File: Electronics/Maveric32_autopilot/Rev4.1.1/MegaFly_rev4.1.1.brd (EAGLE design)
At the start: 69.2 x 38 mm, 115 parts, among them J1 SOLDER_JUMPER_2WAY, J2 SOLDER_JUMPER_2WAY, J3 SOLDER_JUMPER_2WAY, P1 POWER, P10 POWERSMALL_SMD, P11 POWERSMALL_SMD, P12 POWERSMALL_SMD, P13 POWERSMALL_SMD, P2 AVR32_JTAG+SERIALMOLEX_PICOBL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, P5 SPEKTRUM_RECEIVER, P6 SPEKTRUM_RECEIVER, P8 SENSOR, P9 SENSOR, Q1 N-CHANNEL_SOT23, Q2 N-CHANNEL_SOT23, Q3 N-CHANNEL_SOT23, Q4 N-CHANNEL_SOT23, Q5 MOSFET-PCHANNELSMD, U1 LM2734, U10 AT32UC3C1512/1256/1128, U2 MC78L05, U3 V_REG_MIC5235-3.3, U4 LM2734, U50 BMP180, U60 HMC5883L, U70 LSM330DLC, X1 CRYSTAL:ABM_16MHz

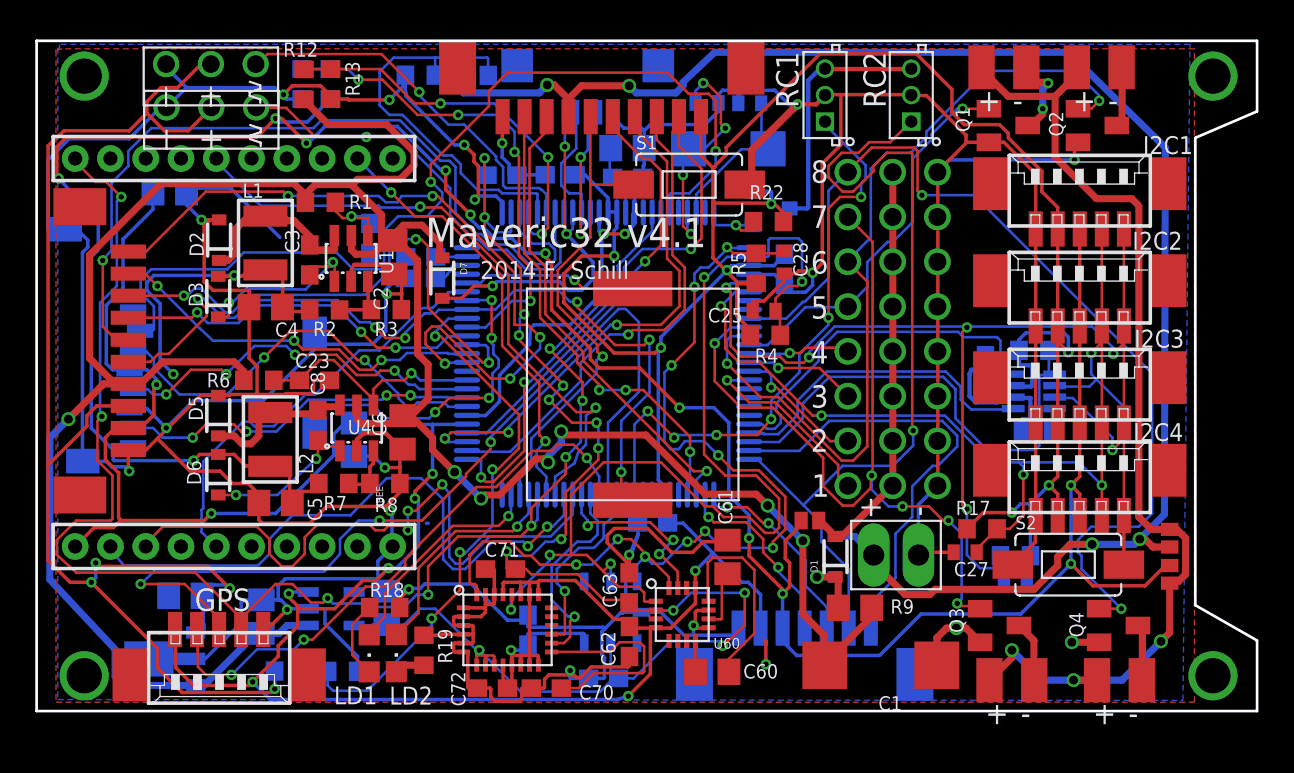
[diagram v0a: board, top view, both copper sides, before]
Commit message: New headers for communication folder of the Library and Update of Electronics for 4.1.1
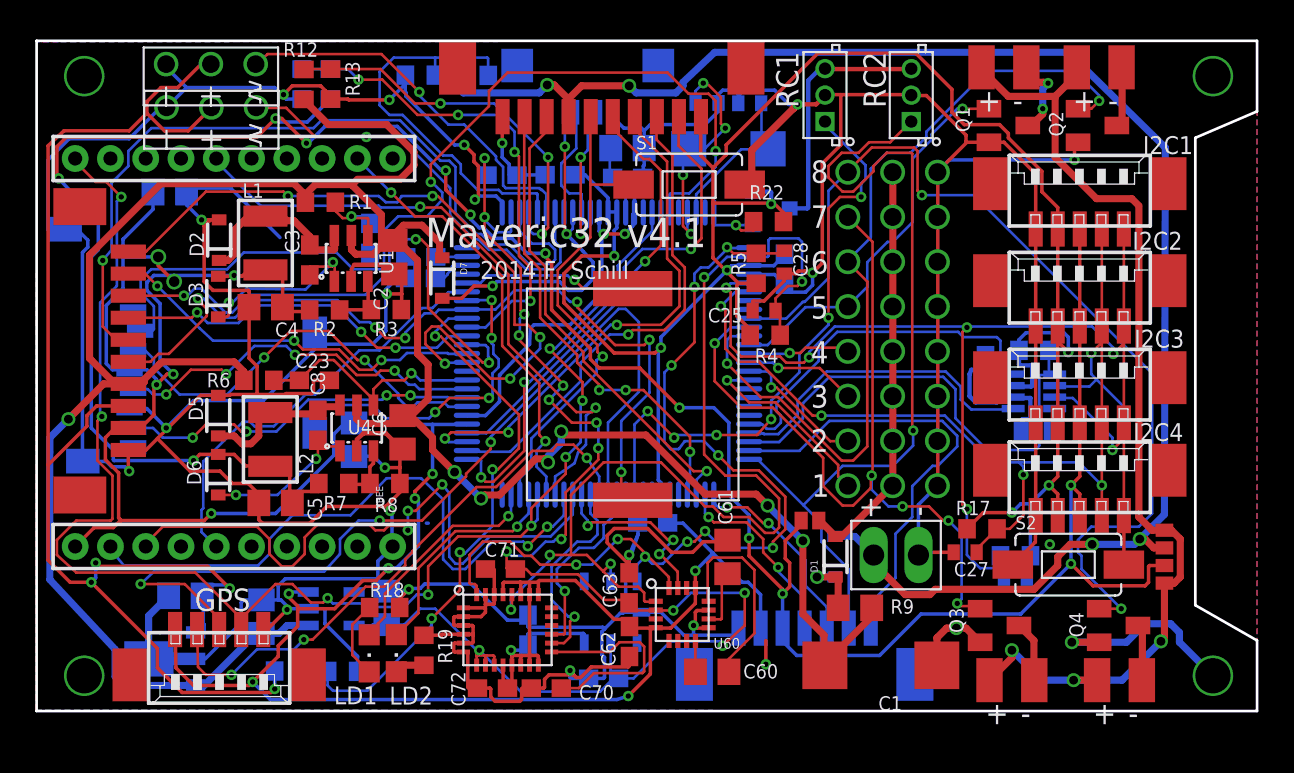
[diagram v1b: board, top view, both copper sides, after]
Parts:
- moved J2 0.30 mm to (63.5, 10.0)
- moved J3 0.30 mm to (63.5, 8.00)
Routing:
- net GND: track 427.8 -> 444.0 mm, vias 27 -> 28
- net +3V3: track 296.3 -> 301.7 mm, vias 19 -> 21
- net BAT_FILTERED: track 149.6 -> 150.6 mm

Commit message: Update wiki and electronics documentation
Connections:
- new net +5V: C5.2, D6.2, J1.P$2, J3.P$2, L2.2, R7.1
- net +6V: no longer C5.2, D6.2, J1.P$2, J3.P$2, L2.2, R7.1
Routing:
- net +6V: track 153.5 -> 142.9 mm
- net +5V: track 0.00 -> 8.54 mm
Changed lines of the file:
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@@
 </signal>
 <signal name="+6V" class="1">
-<contactref element="C5" pad="2"/>
-<contactref element="L2" pad="2"/>
-<contactref element="R7" pad="1"/>
-<contactref element="D6" pad="2"/>
 <contactref element="R20" pad="2"/>
 <contactref element="I2C1" pad="3"/>
@@
 <contactref element="I2C4" pad="3"/>
 <contactref element="SPI" pad="5"/>
-<wire x1="15.55" y1="12.7" x2="15.55" y2="13.15" width="0.2" layer="1"/>
-<wire x1="13.9" y1="12.7" x2="15.55" y2="12.7" width="0.2" layer="1"/>
-<wire x1="10.75" y1="14.8" x2="9.85" y2="14.8" width="0.2" layer="1"/>
-<wire x1="11.4" y1="14.15" x2="10.75" y2="14.8" width="0.2" layer="1"/>
-<wire x1="12.8" y1="14.15" x2="11.4" y2="14.15" width="0.2" layer="1"/>
-<wire x1="12.8" y1="14.15" x2="12.8" y2="14.126" width="0.2" layer="1"/>
 <wire x1="14.9" y1="33.65" x2="16.2" y2="34.95" width="0.2" layer="16"/>
 <wire x1="13.3" y1="33.65" x2="14.9" y2="33.65" width="0.2" layer="16"/>
@@
 <wire x1="8.45" y1="14.45" x2="3.95" y2="14.45" width="0.2" layer="16"/>
 <wire x1="8.8" y1="14.8" x2="8.45" y2="14.45" width="0.2" layer="1"/>
-<wire x1="9.85" y1="14.8" x2="8.8" y2="14.8" width="0.2" layer="1"/>
-<wire x1="13.9" y1="13.9" x2="13.9" y2="12.7" width="0.2" layer="1"/>
-<wire x1="13.9" y1="12.7" x2="14.05" y2="12.05" width="0.2" layer="1"/>
-<wire x1="13.8" y1="14.15" x2="13.9" y2="13.9" width="0.2" layer="1"/>
-<wire x1="12.85" y1="14.15" x2="13.8" y2="14.15" width="0.2" layer="1"/>
-<wire x1="12.85" y1="14.15" x2="12.8" y2="14.126" width="0.2" layer="1"/>
 <wire x1="58.7" y1="27.58" x2="58.7" y2="22.08" width="0.2" layer="1"/>
 <wire x1="58.7" y1="27.8" x2="58.7" y2="27.58" width="0.2" layer="1"/>
@@
 <via x="39.95" y="10.05" extent="1-16" drill="0.3"/>
 <via x="41.85" y="6.9" extent="1-16" drill="0.3"/>
-<contactref element="J3" pad="P$2"/>
-<contactref element="J1" pad="P$2"/>
-<wire x1="42.9" y1="11.05" x2="42.9" y2="10.8" width="0.2" layer="1"/>
 <wire x1="42.9" y1="10.8" x2="42" y2="9.9" width="0.2" layer="1"/>
 <wire x1="42" y1="9.9" x2="42" y2="8.9" width="0.2" layer="1"/>
@@
 <wire x1="58.2" y1="8.6" x2="59.45" y2="7.35" width="0.2" layer="1"/>
 <wire x1="59.45" y1="7.35" x2="62.4" y2="7.35" width="0.2" layer="1"/>
-<wire x1="63.5" y1="8.5" x2="63.55" y2="8.5" width="0.2" layer="1"/>
 <wire x1="47.35" y1="3.4" x2="49.7" y2="5.75" width="0.2" layer="16"/>
 <wire x1="49.7" y1="5.75" x2="55.35" y2="5.75" width="0.2" layer="16"/>
@@
 <wire x1="42.25" y1="7.3" x2="41.85" y2="6.9" width="0.2" layer="1"/>
 <wire x1="41.85" y1="6.9" x2="41.85" y2="7.15" width="0.2" layer="1"/>
-<wire x1="62.65" y1="8.5" x2="63.5" y2="8.5" width="0.2" layer="1"/>
 <wire x1="62.6" y1="8.45" x2="62.65" y2="8.5" width="0.2" layer="1"/>
 <wire x1="62.6" y1="7.55" x2="62.6" y2="8.45" width="0.2" layer="1"/>
@@
 <signal name="N$37">
 </signal>
+<signal name="+5V" class="1">
+<contactref element="C5" pad="2"/>
+<contactref element="L2" pad="2"/>
+<contactref element="R7" pad="1"/>
+<contactref element="D6" pad="2"/>
+<contactref element="J3" pad="P$2"/>
+<contactref element="J1" pad="P$2"/>
+<wire x1="15.55" y1="12.7" x2="15.55" y2="13.15" width="0.2" layer="1"/>
+<wire x1="13.9" y1="12.7" x2="15.55" y2="12.7" width="0.2" layer="1"/>
+<wire x1="10.75" y1="14.8" x2="9.85" y2="14.8" width="0.2" layer="1"/>
+<wire x1="11.4" y1="14.15" x2="10.75" y2="14.8" width="0.2" layer="1"/>
+<wire x1="12.8" y1="14.15" x2="11.4" y2="14.15" width="0.2" layer="1"/>
+<wire x1="12.8" y1="14.15" x2="12.8" y2="14.126" width="0.2" layer="1"/>
+<wire x1="13.9" y1="13.9" x2="13.9" y2="12.7" width="0.2" layer="1"/>
+<wire x1="13.9" y1="12.7" x2="14.05" y2="12.05" width="0.2" layer="1"/>
+<wire x1="13.8" y1="14.15" x2="13.9" y2="13.9" width="0.2" layer="1"/>
+<wire x1="12.85" y1="14.15" x2="13.8" y2="14.15" width="0.2" layer="1"/>
+<wire x1="12.85" y1="14.15" x2="12.8" y2="14.126" width="0.2" layer="1"/>
+<wire x1="63.5" y1="8.5" x2="63.55" y2="8.5" width="0.2" layer="1"/>
+<wire x1="42.9" y1="11.05" x2="63.5" y2="8.5" width="0" layer="19" extent="1-1"/>
+<wire x1="15.55" y1="12.7" x2="42.9" y2="11.05" width="0" layer="19" extent="1-1"/>
+</signal>
 </signals>

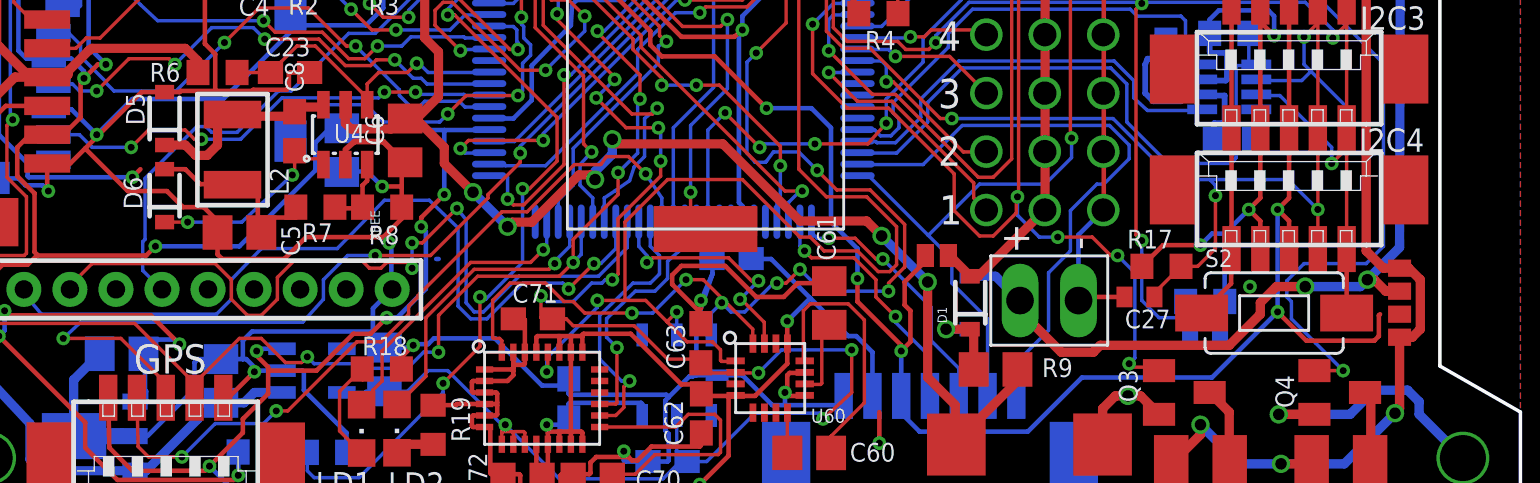
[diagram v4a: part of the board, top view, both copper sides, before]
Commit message: Revert "Update wiki and electronics documentation"
This reverts commit 820a4100233712abf54084fecef851c241c0b9cc.
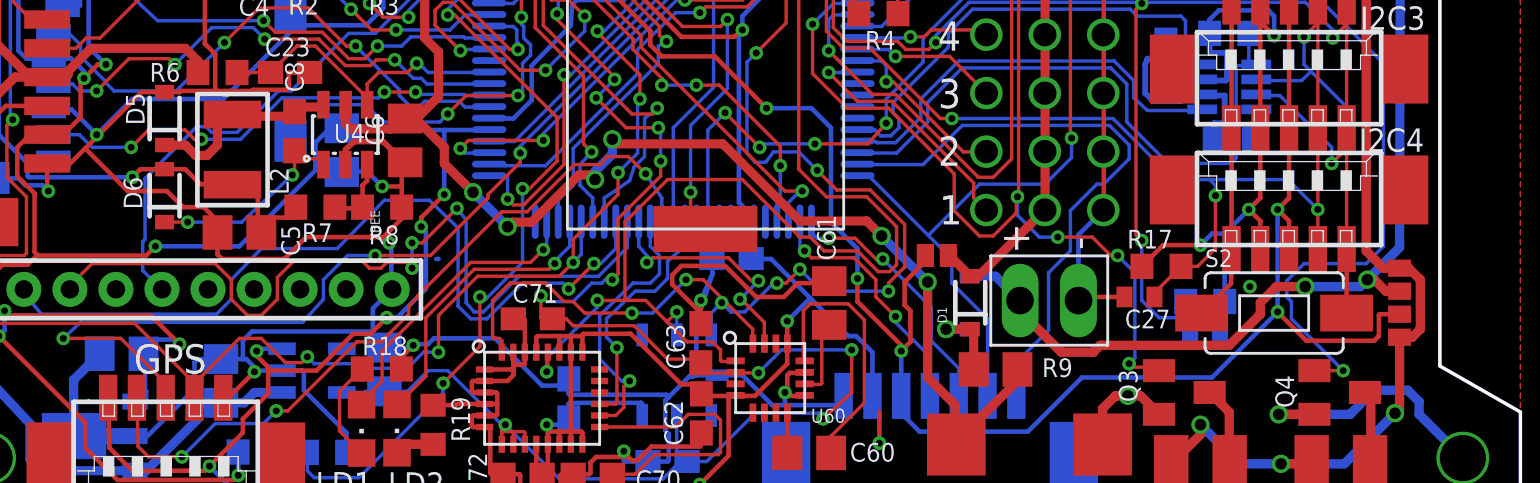
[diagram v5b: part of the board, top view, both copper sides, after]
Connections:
- removed net +5V: C5.2, D6.2, J1.P$2, J3.P$2, L2.2, R7.1
- net +6V: now also C5.2, D6.2, J1.P$2, J3.P$2, L2.2, R7.1
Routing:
- net +6V: track 142.9 -> 153.5 mm
- net +5V: track 8.54 -> 0.00 mm
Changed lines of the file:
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@@
 </signal>
 <signal name="+6V" class="1">
+<contactref element="C5" pad="2"/>
+<contactref element="L2" pad="2"/>
+<contactref element="R7" pad="1"/>
+<contactref element="D6" pad="2"/>
 <contactref element="R20" pad="2"/>
 <contactref element="I2C1" pad="3"/>
@@
 <contactref element="I2C4" pad="3"/>
 <contactref element="SPI" pad="5"/>
+<wire x1="15.55" y1="12.7" x2="15.55" y2="13.15" width="0.2" layer="1"/>
+<wire x1="13.9" y1="12.7" x2="15.55" y2="12.7" width="0.2" layer="1"/>
+<wire x1="10.75" y1="14.8" x2="9.85" y2="14.8" width="0.2" layer="1"/>
+<wire x1="11.4" y1="14.15" x2="10.75" y2="14.8" width="0.2" layer="1"/>
+<wire x1="12.8" y1="14.15" x2="11.4" y2="14.15" width="0.2" layer="1"/>
+<wire x1="12.8" y1="14.15" x2="12.8" y2="14.126" width="0.2" layer="1"/>
 <wire x1="14.9" y1="33.65" x2="16.2" y2="34.95" width="0.2" layer="16"/>
 <wire x1="13.3" y1="33.65" x2="14.9" y2="33.65" width="0.2" layer="16"/>
@@
 <wire x1="8.45" y1="14.45" x2="3.95" y2="14.45" width="0.2" layer="16"/>
 <wire x1="8.8" y1="14.8" x2="8.45" y2="14.45" width="0.2" layer="1"/>
+<wire x1="9.85" y1="14.8" x2="8.8" y2="14.8" width="0.2" layer="1"/>
+<wire x1="13.9" y1="13.9" x2="13.9" y2="12.7" width="0.2" layer="1"/>
+<wire x1="13.9" y1="12.7" x2="14.05" y2="12.05" width="0.2" layer="1"/>
+<wire x1="13.8" y1="14.15" x2="13.9" y2="13.9" width="0.2" layer="1"/>
+<wire x1="12.85" y1="14.15" x2="13.8" y2="14.15" width="0.2" layer="1"/>
+<wire x1="12.85" y1="14.15" x2="12.8" y2="14.126" width="0.2" layer="1"/>
 <wire x1="58.7" y1="27.58" x2="58.7" y2="22.08" width="0.2" layer="1"/>
 <wire x1="58.7" y1="27.8" x2="58.7" y2="27.58" width="0.2" layer="1"/>
@@
 <via x="39.95" y="10.05" extent="1-16" drill="0.3"/>
 <via x="41.85" y="6.9" extent="1-16" drill="0.3"/>
+<contactref element="J3" pad="P$2"/>
+<contactref element="J1" pad="P$2"/>
+<wire x1="42.9" y1="11.05" x2="42.9" y2="10.8" width="0.2" layer="1"/>
 <wire x1="42.9" y1="10.8" x2="42" y2="9.9" width="0.2" layer="1"/>
 <wire x1="42" y1="9.9" x2="42" y2="8.9" width="0.2" layer="1"/>
@@
 <wire x1="58.2" y1="8.6" x2="59.45" y2="7.35" width="0.2" layer="1"/>
 <wire x1="59.45" y1="7.35" x2="62.4" y2="7.35" width="0.2" layer="1"/>
+<wire x1="63.5" y1="8.5" x2="63.55" y2="8.5" width="0.2" layer="1"/>
 <wire x1="47.35" y1="3.4" x2="49.7" y2="5.75" width="0.2" layer="16"/>
 <wire x1="49.7" y1="5.75" x2="55.35" y2="5.75" width="0.2" layer="16"/>
@@
 <wire x1="42.25" y1="7.3" x2="41.85" y2="6.9" width="0.2" layer="1"/>
 <wire x1="41.85" y1="6.9" x2="41.85" y2="7.15" width="0.2" layer="1"/>
+<wire x1="62.65" y1="8.5" x2="63.5" y2="8.5" width="0.2" layer="1"/>
 <wire x1="62.6" y1="8.45" x2="62.65" y2="8.5" width="0.2" layer="1"/>
 <wire x1="62.6" y1="7.55" x2="62.6" y2="8.45" width="0.2" layer="1"/>
@@
 <signal name="N$37">
 </signal>
-<signal name="+5V" class="1">
-<contactref element="C5" pad="2"/>
-<contactref element="L2" pad="2"/>
-<contactref element="R7" pad="1"/>
-<contactref element="D6" pad="2"/>
-<contactref element="J3" pad="P$2"/>
-<contactref element="J1" pad="P$2"/>
-<wire x1="15.55" y1="12.7" x2="15.55" y2="13.15" width="0.2" layer="1"/>
-<wire x1="13.9" y1="12.7" x2="15.55" y2="12.7" width="0.2" layer="1"/>
-<wire x1="10.75" y1="14.8" x2="9.85" y2="14.8" width="0.2" layer="1"/>
-<wire x1="11.4" y1="14.15" x2="10.75" y2="14.8" width="0.2" layer="1"/>
-<wire x1="12.8" y1="14.15" x2="11.4" y2="14.15" width="0.2" layer="1"/>
-<wire x1="12.8" y1="14.15" x2="12.8" y2="14.126" width="0.2" layer="1"/>
-<wire x1="13.9" y1="13.9" x2="13.9" y2="12.7" width="0.2" layer="1"/>
-<wire x1="13.9" y1="12.7" x2="14.05" y2="12.05" width="0.2" layer="1"/>
-<wire x1="13.8" y1="14.15" x2="13.9" y2="13.9" width="0.2" layer="1"/>
-<wire x1="12.85" y1="14.15" x2="13.8" y2="14.15" width="0.2" layer="1"/>
-<wire x1="12.85" y1="14.15" x2="12.8" y2="14.126" width="0.2" layer="1"/>
-<wire x1="63.5" y1="8.5" x2="63.55" y2="8.5" width="0.2" layer="1"/>
-<wire x1="42.9" y1="11.05" x2="63.5" y2="8.5" width="0" layer="19" extent="1-1"/>
-<wire x1="15.55" y1="12.7" x2="42.9" y2="11.05" width="0" layer="19" extent="1-1"/>
-</signal>
 </signals>
